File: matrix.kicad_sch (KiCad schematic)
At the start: 134 parts, among them SW10 #8, SW11 #9, SW12 #0, SW13 -, SW14 =, SW15 BACKSPACE, SW16 M1, SW17 TAB, SW18 Q, SW19 W, SW2 ESC, SW20 E, SW21 R, SW22 T, SW23 Y, SW24 U, SW25 I, SW26 O, SW27 P, SW28 [, SW29 ], SW3 #1, SW30 \, SW31 M2, SW32 CAPS, SW33 A, SW34 S, SW35 D, SW36 F, SW37 G, SW38 H, SW39 J, SW4 #2, SW40 K, SW41 L, SW42 ;, SW43 ', SW44 ENTER, SW45 M3, SW46 LSHIFT, SW47 Z, SW48 X, SW49 C, SW5 #3, SW50 V, SW51 B, SW52 N, SW53 M, SW54 ,, SW55 ., SW56 /, SW57 RSHIFT, SW58 UPARROW, SW59 M3, SW6 #4, SW60 LCTRL, SW61 WINDOWS, SW62 LALT, SW63 SPACE, SW64 RALT, SW65 RCTRL, SW66 LEFTARROW, SW67 DOWNARROW, SW68 RIGHTARROW, SW7 #5, SW8 #6, SW9 #7

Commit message: PCB start, schematic mostly finished
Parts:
- D10, D11, D12, D13, D14, D15, D16, D17, D18, D19, D2, D20, D21, D22, D23, D24, D25, D26, D27, D28, D29, D3, D30, D31, D32, D33, D34, D35, D36, D37, D38, D39, D4, D40, D41, D42, D43, D44, D45, D46, D47, D48, D49, D5, D50, D51, D52, D53, D54, D55, D56, D57, D58, D59, D6, D60, D61, D62, D63, D64, D65, D66, D67, D68, D7, D8, D9: footprint (none) -> Diode_SMD:D_SOD-123
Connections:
- net COL0: no longer D10.1 (K), D11.1 (K), D12.1 (K), D13.1 (K), D14.1 (K), D15.1 (K), D16.1 (K), D17.1 (K), D18.1 (K), D19.1 (K), D2.1 (K), D20.1 (K), D21.1 (K), D22.1 (K), D23.1 (K), D24.1 (K), D25.1 (K), D26.1 (K), D27.1 (K), D28.1 (K), D29.1 (K), D3.1 (K), D30.1 (K), D31.1 (K), D32.1 (K), D33.1 (K), D34.1 (K), D35.1 (K), D36.1 (K), D37.1 (K), D38.1 (K), D39.1 (K), D4.1 (K), D40.1 (K), D41.1 (K), D42.1 (K), D43.1 (K), D44.1 (K), D45.1 (K), D46.1 (K), D47.1 (K), D48.1 (K), D49.1 (K), D5.1 (K), D50.1 (K), D51.1 (K), D52.1 (K), D53.1 (K), D54.1 (K), D55.1 (K), D56.1 (K), D57.1 (K), D58.1 (K), D59.1 (K), D6.1 (K), D60.1 (K), D61.1 (K), D62.1 (K), D63.1 (K), D64.1 (K), D65.1 (K), D66.1 (K), D67.1 (K), D68.1 (K), D7.1 (K), D8.1 (K), D9.1 (K), SW10.1, SW11.1, SW12.1, SW13.1, SW14.1, SW15.1, SW16.1, SW18.1, SW19.1, SW20.1, SW21.1, SW22.1, SW23.1, SW24.1, SW25.1, SW26.1, SW27.1, SW28.1, SW29.1, SW3.1, SW30.1, SW31.1, SW33.1, SW34.1, SW35.1, SW36.1, SW37.1, SW38.1, SW39.1, SW4.1, SW40.1, SW41.1, SW42.1, SW43.1, SW44.1, SW45.1, SW47.1, SW48.1, SW49.1, SW5.1, SW50.1, SW51.1, SW52.1, SW53.1, SW54.1, SW55.1, SW56.1, SW57.1, SW58.1, SW59.1, SW6.1, SW61.1, SW62.1, SW63.1, SW64.1, SW65.1, SW66.1, SW67.1, SW68.1, SW7.1, SW8.1, SW9.1
- new net COL1: SW18.1, SW3.1, SW33.1, SW47.1, SW61.1
- new net COL10: SW12.1, SW27.1, SW42.1, SW56.1, SW64.1
- new net COL11: SW13.1, SW28.1, SW43.1, SW65.1
- new net COL12: SW14.1, SW29.1, SW57.1, SW66.1
- new net COL13: SW15.1, SW30.1, SW44.1, SW58.1, SW67.1
- new net COL14: SW16.1, SW31.1, SW45.1, SW59.1, SW68.1
- new net COL2: SW19.1, SW34.1, SW4.1, SW48.1, SW62.1
- new net COL3: SW20.1, SW35.1, SW49.1, SW5.1
- new net COL4: SW21.1, SW36.1, SW50.1, SW6.1
- new net COL5: SW22.1, SW37.1, SW51.1, SW7.1
- new net COL6: SW23.1, SW38.1, SW52.1, SW63.1, SW8.1
- new net COL7: SW24.1, SW39.1, SW53.1, SW9.1
- new net COL8: SW10.1, SW25.1, SW40.1, SW54.1
- new net COL9: SW11.1, SW26.1, SW41.1, SW55.1
- new net ROW0: D10.1 (K), D11.1 (K), D12.1 (K), D13.1 (K), D14.1 (K), D15.1 (K), D16.1 (K), D2.1 (K), D3.1 (K), D4.1 (K), D5.1 (K), D6.1 (K), D7.1 (K), D8.1 (K), D9.1 (K)
- new net ROW1: D17.1 (K), D18.1 (K), D19.1 (K), D20.1 (K), D21.1 (K), D22.1 (K), D23.1 (K), D24.1 (K), D25.1 (K), D26.1 (K), D27.1 (K), D28.1 (K), D29.1 (K), D30.1 (K), D31.1 (K)
- new net ROW2: D32.1 (K), D33.1 (K), D34.1 (K), D35.1 (K), D36.1 (K), D37.1 (K), D38.1 (K), D39.1 (K), D40.1 (K), D41.1 (K), D42.1 (K), D43.1 (K), D44.1 (K), D45.1 (K)
- new net ROW3: D46.1 (K), D47.1 (K), D48.1 (K), D49.1 (K), D50.1 (K), D51.1 (K), D52.1 (K), D53.1 (K), D54.1 (K), D55.1 (K), D56.1 (K), D57.1 (K), D58.1 (K), D59.1 (K)
- new net ROW4: D60.1 (K), D61.1 (K), D62.1 (K), D63.1 (K), D64.1 (K), D65.1 (K), D66.1 (K), D67.1 (K), D68.1 (K)

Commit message: PCB Outline
Switches placed in correct areas mostly. Still need to route and place components.
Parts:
- SW17, SW30: footprint marbastlib-mx:SW_MX_1u -> marbastlib-mx:SW_MX_1.5u
- SW32, SW57: footprint marbastlib-mx:SW_MX_1u -> marbastlib-mx:SW_MX_1.75u
- SW60, SW61, SW62, SW64, SW65: footprint marbastlib-mx:SW_MX_1u -> marbastlib-mx:SW_MX_1.25u
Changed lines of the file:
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@@
     (property "Reference" "SW17" (id 0) (at 41.148 44.196 0))
     (property "Value" "TAB" (id 1) (at 41.148 46.736 0))
-    (property "Footprint" "marbastlib-mx:SW_MX_1u" (id 2) (at 35.814 51.054 0)
+    (property "Footprint" "marbastlib-mx:SW_MX_1.5u" (id 2) (at 35.814 51.054 0)
       (effects (font (size 1.27 1.27)) hide)
     )
@@
     (property "Reference" "SW65" (id 0) (at 208.534 86.868 0))
     (property "Value" "RCTRL" (id 1) (at 208.534 89.408 0))
-    (property "Footprint" "marbastlib-mx:SW_MX_1u" (id 2) (at 203.2 93.726 0)
+    (property "Footprint" "marbastlib-mx:SW_MX_1.25u" (id 2) (at 203.2 93.726 0)
       (effects (font (size 1.27 1.27)) hide)
     )
@@
     (property "Reference" "SW30" (id 0) (at 239.014 44.196 0))
     (property "Value" "\\" (id 1) (at 239.014 46.736 0))
-    (property "Footprint" "marbastlib-mx:SW_MX_1u" (id 2) (at 233.68 51.054 0)
+    (property "Footprint" "marbastlib-mx:SW_MX_1.5u" (id 2) (at 233.68 51.054 0)
       (effects (font (size 1.27 1.27)) hide)
     )
@@
     (property "Reference" "SW32" (id 0) (at 40.894 58.42 0))
     (property "Value" "CAPS" (id 1) (at 40.894 60.96 0))
-    (property "Footprint" "marbastlib-mx:SW_MX_1u" (id 2) (at 35.56 65.278 0)
+    (property "Footprint" "marbastlib-mx:SW_MX_1.75u" (id 2) (at 35.56 65.278 0)
       (effects (font (size 1.27 1.27)) hide)
     )
@@
     (property "Reference" "SW61" (id 0) (at 56.134 86.868 0))
     (property "Value" "WINDOWS" (id 1) (at 56.134 89.408 0))
-    (property "Footprint" "marbastlib-mx:SW_MX_1u" (id 2) (at 50.8 93.726 0)
+    (property "Footprint" "marbastlib-mx:SW_MX_1.25u" (id 2) (at 50.8 93.726 0)
       (effects (font (size 1.27 1.27)) hide)
     )
@@
     (property "Reference" "SW57" (id 0) (at 223.774 72.644 0))
     (property "Value" "RSHIFT" (id 1) (at 223.774 75.184 0))
-    (property "Footprint" "marbastlib-mx:SW_MX_1u" (id 2) (at 218.44 79.502 0)
+    (property "Footprint" "marbastlib-mx:SW_MX_1.75u" (id 2) (at 218.44 79.502 0)
       (effects (font (size 1.27 1.27)) hide)
     )
@@
     (property "Reference" "SW60" (id 0) (at 40.894 86.868 0))
     (property "Value" "LCTRL" (id 1) (at 40.894 89.408 0))
-    (property "Footprint" "marbastlib-mx:SW_MX_1u" (id 2) (at 35.56 93.726 0)
+    (property "Footprint" "marbastlib-mx:SW_MX_1.25u" (id 2) (at 35.56 93.726 0)
       (effects (font (size 1.27 1.27)) hide)
     )
@@
     (property "Reference" "SW64" (id 0) (at 193.294 86.868 0))
     (property "Value" "RALT" (id 1) (at 193.294 89.408 0))
-    (property "Footprint" "marbastlib-mx:SW_MX_1u" (id 2) (at 187.96 93.726 0)
+    (property "Footprint" "marbastlib-mx:SW_MX_1.25u" (id 2) (at 187.96 93.726 0)
       (effects (font (size 1.27 1.27)) hide)
     )
@@
     (property "Reference" "SW62" (id 0) (at 71.374 86.868 0))
     (property "Value" "LALT" (id 1) (at 71.374 89.408 0))
-    (property "Footprint" "marbastlib-mx:SW_MX_1u" (id 2) (at 66.04 93.726 0)
-      (effects (font (size 1.27 1.27)) hide)
-    )
+    (property "Footprint" "marbastlib-mx:SW_MX_1.25u" (id 2) (at 66.04 93.726 0)
+      (effects (font (size 1.27 1.27)) hide)
+    )

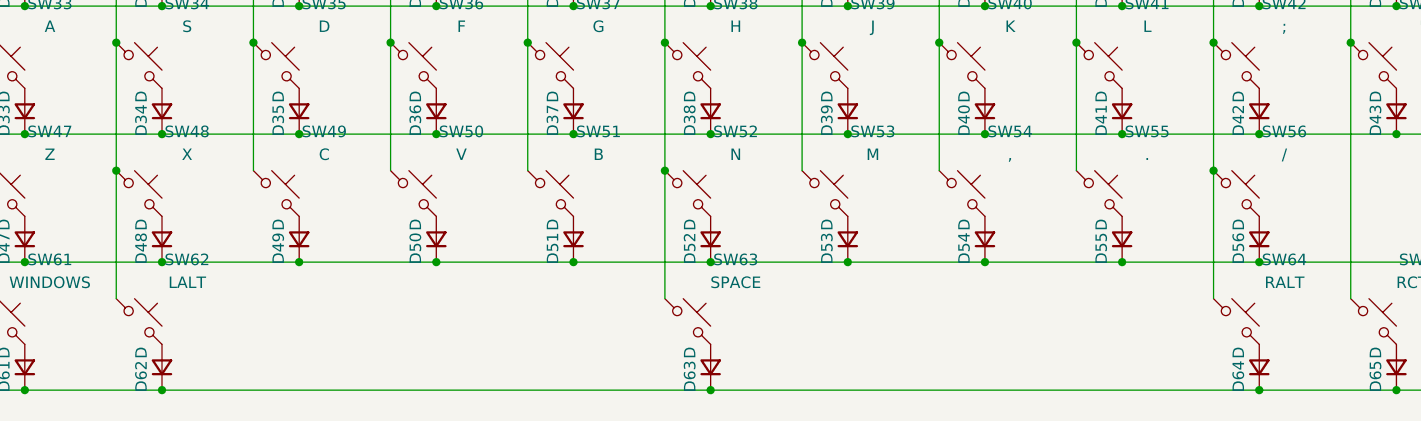
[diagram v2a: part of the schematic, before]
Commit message: rerouted pcb
fixing drc issues
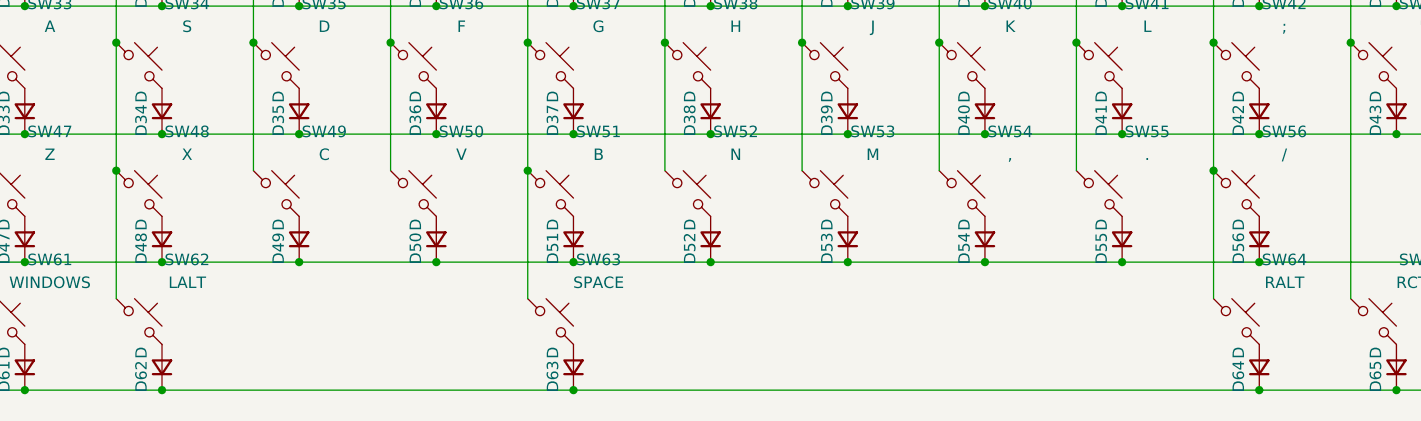
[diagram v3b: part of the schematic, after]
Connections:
- net COL5: now also SW63.1
- net COL6: no longer SW63.1
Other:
- moved on the sheet: D63, SW63
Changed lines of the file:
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@@
   (junction (at 38.1 72.898) (diameter 0) (color 0 0 0 0)
   )
+  (junction (at 114.3 101.346) (diameter 0) (color 0 0 0 0)
+  )
   (junction (at 139.7 62.738) (diameter 0) (color 0 0 0 0)
   )
@@
   (junction (at 236.22 101.346) (diameter 0) (color 0 0 0 0)
   )
+  (junction (at 109.22 76.962) (diameter 0) (color 0 0 0 0)
+  )
   (junction (at 160.02 72.898) (diameter 0) (color 0 0 0 0)
   )
@@
   (junction (at 220.98 58.674) (diameter 0) (color 0 0 0 0)
   )
-  (junction (at 129.54 101.346) (diameter 0) (color 0 0 0 0)
-  )
   (junction (at 48.26 48.514) (diameter 0) (color 0 0 0 0)
   )
@@
   (junction (at 170.18 62.738) (diameter 0) (color 0 0 0 0)
   )
-  (junction (at 124.46 76.962) (diameter 0) (color 0 0 0 0)
-  )
   (junction (at 175.26 58.674) (diameter 0) (color 0 0 0 0)
   )
@@
     (stroke (width 0) (type default) (color 0 0 0 0))
   )
-  (wire (pts (xy 68.58 101.346) (xy 129.54 101.346))
-    (stroke (width 0) (type default) (color 0 0 0 0))
-  )
   (wire (pts (xy 99.06 72.898) (xy 114.3 72.898))
     (stroke (width 0) (type default) (color 0 0 0 0))
@@
     (stroke (width 0) (type default) (color 0 0 0 0))
   )
-  (wire (pts (xy 129.54 101.346) (xy 190.5 101.346))
+  (wire (pts (xy 68.58 101.346) (xy 114.3 101.346))
     (stroke (width 0) (type default) (color 0 0 0 0))
   )
@@
     (stroke (width 0) (type default) (color 0 0 0 0))
   )
+  (wire (pts (xy 114.3 101.346) (xy 190.5 101.346))
+    (stroke (width 0) (type default) (color 0 0 0 0))
+  )
   (wire (pts (xy 109.22 48.514) (xy 109.22 62.738))
     (stroke (width 0) (type default) (color 0 0 0 0))
@@
     (stroke (width 0) (type default) (color 0 0 0 0))
   )
-  (wire (pts (xy 124.46 76.962) (xy 124.46 91.186))
+  (wire (pts (xy 109.22 76.962) (xy 109.22 91.186))
     (stroke (width 0) (type default) (color 0 0 0 0))
   )
@@
     (pin "2")
   )
-  (symbol (lib_id "marbastlib-mx:MX_SW_solder") (at 127 93.726 0) (unit 1)
-    (in_bom yes) (on_board yes)
-    (property "Reference" "SW63" (id 0) (at 132.334 86.868 0))
-    (property "Value" "SPACE" (id 1) (at 132.334 89.408 0))
-    (property "Footprint" "marbastlib-mx:SW_MX_1u" (id 2) (at 127 93.726 0)
-      (effects (font (size 1.27 1.27)) hide)
-    )
-    (property "Datasheet" "~" (id 3) (at 127 93.726 0)
+  (symbol (lib_id "marbastlib-mx:MX_SW_solder") (at 111.76 93.726 0) (unit 1)
+    (in_bom yes) (on_board yes)
+    (property "Reference" "SW63" (id 0) (at 117.094 86.868 0))
+    (property "Value" "SPACE" (id 1) (at 117.094 89.408 0))
+    (property "Footprint" "marbastlib-mx:SW_MX_1u" (id 2) (at 111.76 93.726 0)
+      (effects (font (size 1.27 1.27)) hide)
+    )
+    (property "Datasheet" "~" (id 3) (at 111.76 93.726 0)
       (effects (font (size 1.27 1.27)) hide)
     )
@@
     (pin "2")
   )
-  (symbol (lib_id "Device:D_Small") (at 129.54 98.806 90) (unit 1)
-    (in_bom yes) (on_board yes)
-    (property "Reference" "D63" (id 0) (at 127.254 98.044 0)
-      (effects (font (size 1.27 1.27)) (justify right))
-    )
-    (property "Value" "D" (id 1) (at 127.254 96.52 0)
-      (effects (font (size 1.27 1.27)) (justify right))
-    )
-    (property "Footprint" "Diode_SMD:D_SOD-123" (id 2) (at 129.54 98.806 90)
-      (effects (font (size 1.27 1.27)) hide)
-    )
-    (property "Datasheet" "~" (id 3) (at 129.54 98.806 90)
-      (effects (font (size 1.27 1.27)) hide)
-    )
+  (symbol (lib_id "Device:D_Small") (at 114.3 98.806 90) (unit 1)
+    (in_bom yes) (on_board yes)
+    (property "Reference" "D63" (id 0) (at 112.014 98.044 0)
+      (effects (font (size 1.27 1.27)) (justify right))
+    )
+    (property "Value" "D" (id 1) (at 112.014 96.52 0)
+      (effects (font (size 1.27 1.27)) (justify right))
+    )
+    (property "Footprint" "Diode_SMD:D_SOD-123" (id 2) (at 114.3 98.806 90)
+      (effects (font (size 1.27 1.27)) hide)
+    )
+    (property "Datasheet" "~" (id 3) (at 114.3 98.806 90)
+      (effects (font (size 1.27 1.27)) hide)
+    )
